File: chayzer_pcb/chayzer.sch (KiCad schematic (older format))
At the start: 30 parts, among them U1 ProMicro

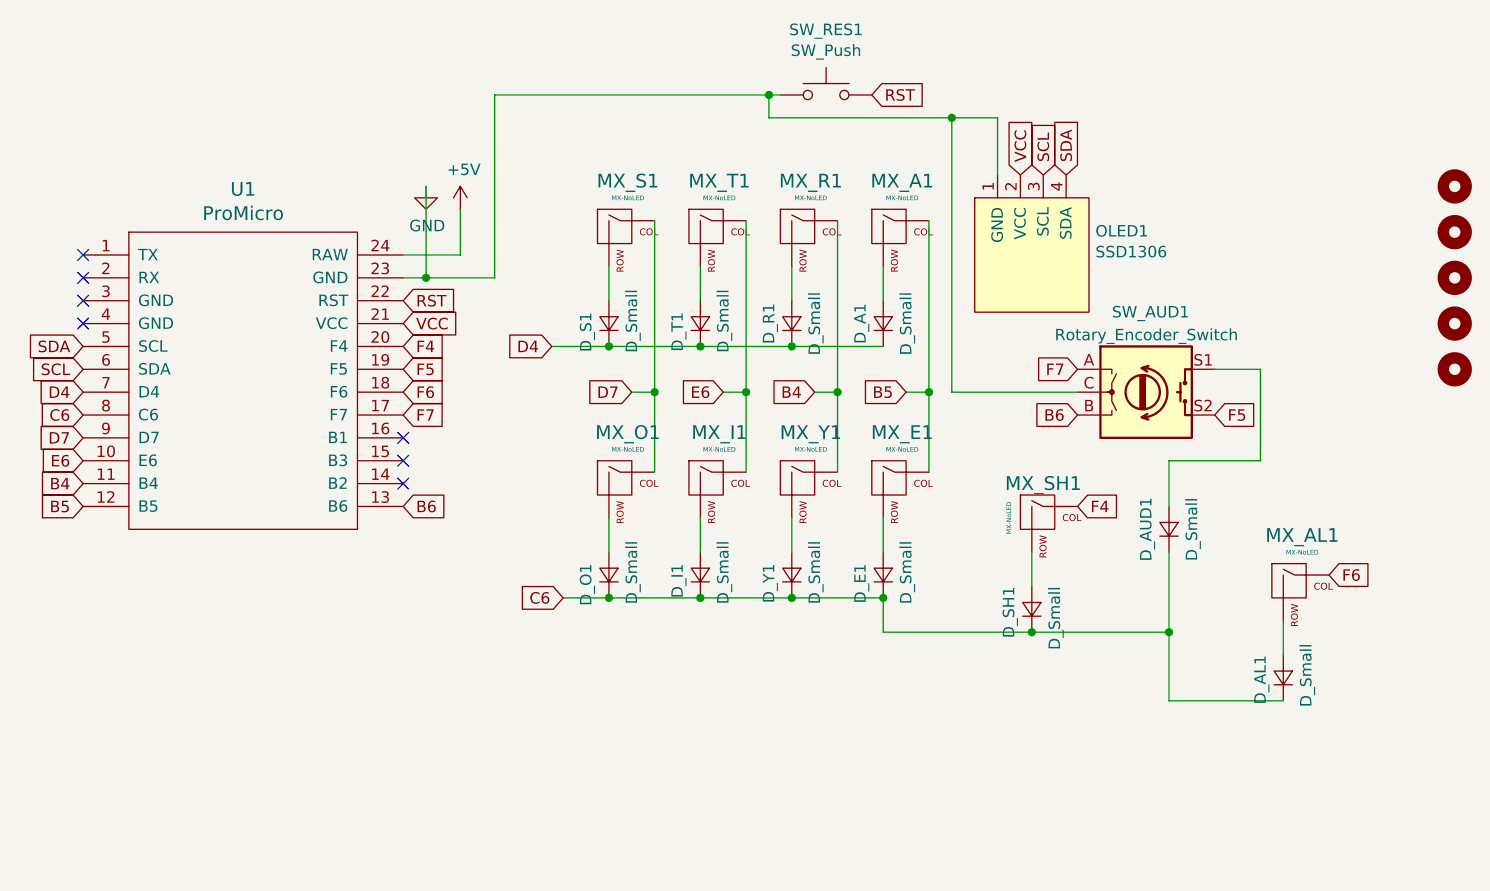
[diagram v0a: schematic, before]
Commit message: added rgb to PCB, buggy in qmk right now, and untested on PCB
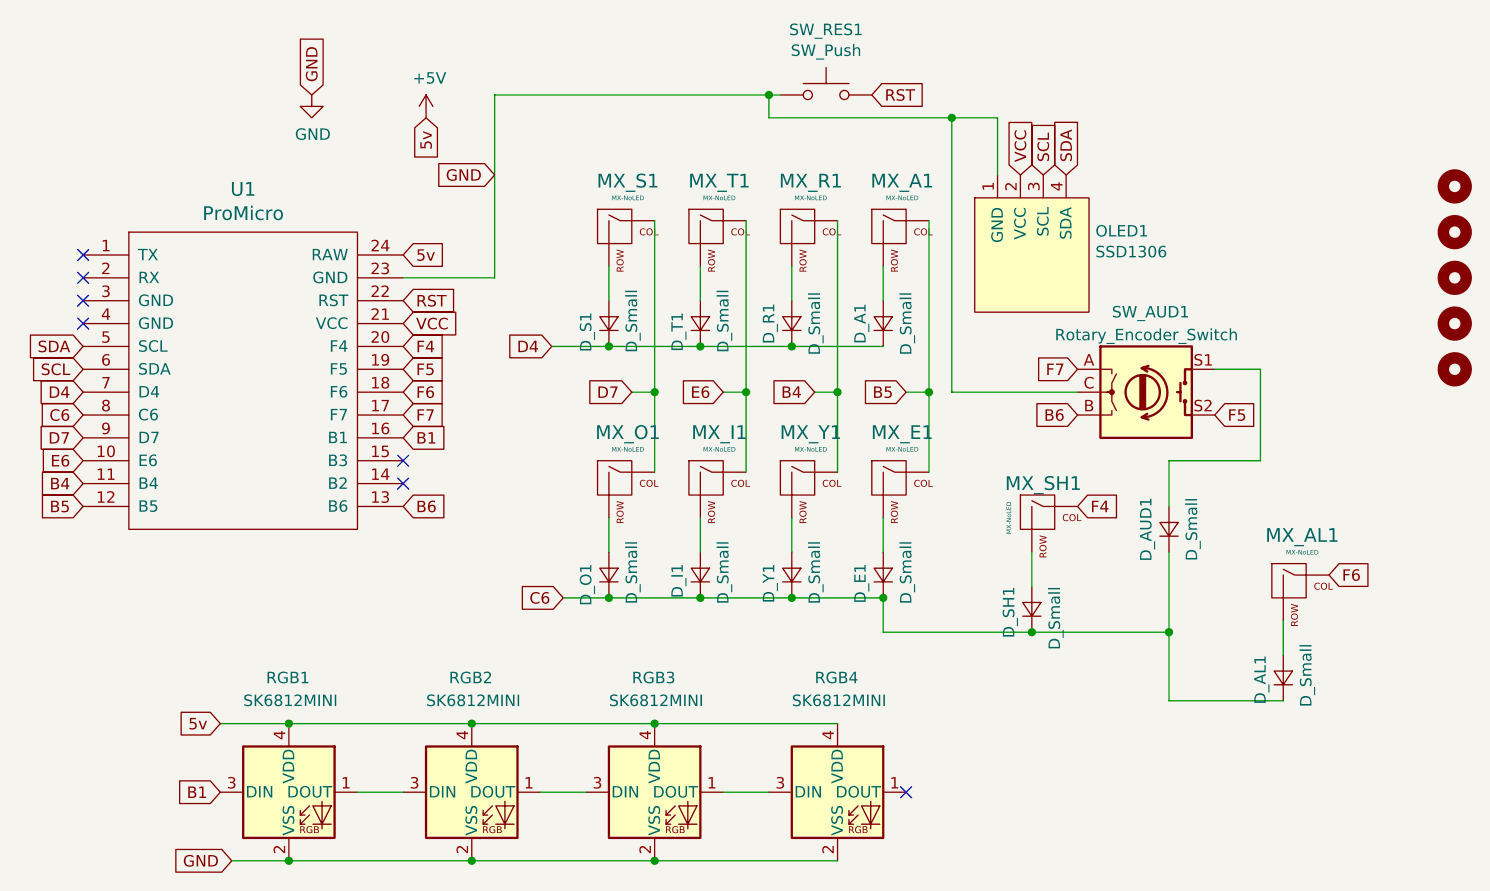
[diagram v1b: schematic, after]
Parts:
- added RGB1, RGB2, RGB3, RGB4: SK6812MINI, LED_SMD:LED_SK6812MINI_PLCC4_3.5x3.5mm_P1.75mm, symbol LED:SK6812MINI
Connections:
- net +5V: now also RGB1.4 (VDD), RGB2.4 (VDD), RGB3.4 (VDD), RGB4.4 (VDD)
- net GND: now also RGB1.2 (VSS), RGB2.2 (VSS), RGB3.2 (VSS), RGB4.2 (VSS)
- net B1: now reaches U1.16 (B1)
- net B1: now also RGB1.3 (DIN)
- new net: RGB1.1 (DOUT), RGB2.3 (DIN)
- new net: RGB2.1 (DOUT), RGB3.3 (DIN)
- new net: RGB3.1 (DOUT), RGB4.3 (DIN)
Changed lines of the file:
@@
 EESchema Schematic File Version 4
+LIBS:chayzer-cache
 EELAYER 30 0
 EELAYER END
@@
 $EndDescr
 $Comp
-L power:+5V #PWR0101
-U 1 1 60D53ACC
-P 4700 3000
-F 0 "#PWR0101" H 4700 2850 50  0001 C CNN
-F 1 "+5V" H 4715 3173 50  0000 C CNN
-F 2 "" H 4700 3000 50  0001 C CNN
-F 3 "" H 4700 3000 50  0001 C CNN
-	1    4700 3000
-	1    0    0    -1
-$EndComp
-$Comp
 L chayzer-rescue:ProMicro-promicro U1
 U 1 1 60D57CF4
@@
 L power:GND #PWR0102
 U 1 1 60D5522F
-P 4550 2900
-F 0 "#PWR0102" H 4550 2650 50  0001 C CNN
-F 1 "GND" H 4555 2727 50  0000 C CNN
-F 2 "" H 4550 2900 50  0001 C CNN
-F 3 "" H 4550 2900 50  0001 C CNN
-	1    4550 2900
-	1    0    0    -1
-$EndComp
-Wire Wire Line
-	4700 3000 4700 3200
-Wire Wire Line
-	4700 3200 4450 3200
+P 4050 2500
+F 0 "#PWR0102" H 4050 2250 50  0001 C CNN
+F 1 "GND" H 4055 2327 50  0000 C CNN
+F 2 "" H 4050 2500 50  0001 C CNN
+F 3 "" H 4050 2500 50  0001 C CNN
+	1    4050 2500
+	1    0    0    -1
+$EndComp
 $Comp
 L chayzer-rescue:MX-NoLED-MX_Alps_Hybrid MX_S1
@@
 	6050 2500 4850 2500
 Wire Wire Line
-	4450 3300 4550 3300
-Wire Wire Line
-	4550 2900 4550 3300
-Connection ~ 4550 3300
-Wire Wire Line
-	4550 3300 4850 3300
-Wire Wire Line
 	5350 3250 5350 3400
 Wire Wire Line
@@
 NoConn ~ 4450 4200
 NoConn ~ 4450 4100
-NoConn ~ 4450 4000
 Wire Wire Line
 	5100 3600 5350 3600
@@
 Text GLabel 4450 4300 2    50   Input ~ 0
 B6
+$Comp
+L LED:SK6812MINI RGB1
+U 1 1 61032E51
+P 3950 5550
+F 0 "RGB1" H 3850 6050 50  0000 L CNN
+F 1 "SK6812MINI" H 3750 5950 50  0000 L CNN
+F 2 "LED_SMD:LED_SK6812MINI_PLCC4_3.5x3.5mm_P1.75mm" H 4000 5250 50  0001 L TNN
+F 3 "https://cdn-shop.adafruit.com/product-files/2686/SK6812MINI_REV.01-1-2.pdf" H 4050 5175 50  0001 L TNN
+	1    3950 5550
+	1    0    0    -1
+$EndComp
+Wire Wire Line
+	4450 3300 4850 3300
+$Comp
+L power:+5V #PWR0101
+U 1 1 60D53ACC
+P 4550 2600
+F 0 "#PWR0101" H 4550 2450 50  0001 C CNN
+F 1 "+5V" H 4565 2773 50  0000 C CNN
+F 2 "" H 4550 2600 50  0001 C CNN
+F 3 "" H 4550 2600 50  0001 C CNN
+	1    4550 2600
+	1    0    0    -1
+$EndComp
+Text GLabel 4450 3200 2    50   Input ~ 0
+5v
+Text GLabel 4850 2850 0    50   Input ~ 0
+GND
+Text GLabel 4550 2600 3    50   Input ~ 0
+5v
+Text GLabel 4050 2500 1    50   Input ~ 0
+GND
+$Comp
+L LED:SK6812MINI RGB2
+U 1 1 6103E43F
+P 4750 5550
+F 0 "RGB2" H 4650 6050 50  0000 L CNN
+F 1 "SK6812MINI" H 4550 5950 50  0000 L CNN
+F 2 "LED_SMD:LED_SK6812MINI_PLCC4_3.5x3.5mm_P1.75mm" H 4800 5250 50  0001 L TNN
+F 3 "https://cdn-shop.adafruit.com/product-files/2686/SK6812MINI_REV.01-1-2.pdf" H 4850 5175 50  0001 L TNN
+	1    4750 5550
+	1    0    0    -1
+$EndComp
+$Comp
+L LED:SK6812MINI RGB3
+U 1 1 6103F28F
+P 5550 5550
+F 0 "RGB3" H 5450 6050 50  0000 L CNN
+F 1 "SK6812MINI" H 5350 5950 50  0000 L CNN
+F 2 "LED_SMD:LED_SK6812MINI_PLCC4_3.5x3.5mm_P1.75mm" H 5600 5250 50  0001 L TNN
+F 3 "https://cdn-shop.adafruit.com/product-files/2686/SK6812MINI_REV.01-1-2.pdf" H 5650 5175 50  0001 L TNN
+	1    5550 5550
+	1    0    0    -1
+$EndComp
+$Comp
+L LED:SK6812MINI RGB4
+U 1 1 6103FF53
+P 6350 5550
+F 0 "RGB4" H 6250 6050 50  0000 L CNN
+F 1 "SK6812MINI" H 6150 5950 50  0000 L CNN
+F 2 "LED_SMD:LED_SK6812MINI_PLCC4_3.5x3.5mm_P1.75mm" H 6400 5250 50  0001 L TNN
+F 3 "https://cdn-shop.adafruit.com/product-files/2686/SK6812MINI_REV.01-1-2.pdf" H 6450 5175 50  0001 L TNN
+	1    6350 5550
+	1    0    0    -1
+$EndComp
+Text GLabel 4450 4000 2    50   Input ~ 0
+B1
+Text GLabel 3650 5550 0    50   Input ~ 0
+B1
+Wire Wire Line
+	4250 5550 4450 5550
+Wire Wire Line
+	5050 5550 5250 5550
+Wire Wire Line
+	5850 5550 6050 5550
+NoConn ~ 6650 5550
+Text GLabel 3700 5850 0    50   Input ~ 0
+GND
+Wire Wire Line
+	3700 5850 3950 5850
+Connection ~ 3950 5850
+Wire Wire Line
+	3950 5850 4750 5850
+Connection ~ 4750 5850
+Wire Wire Line
+	4750 5850 5550 5850
+Connection ~ 5550 5850
+Wire Wire Line
+	5550 5850 6350 5850
+Text GLabel 3650 5250 0    50   Input ~ 0
+5v
+Wire Wire Line
+	3650 5250 3950 5250
+Connection ~ 3950 5250
+Wire Wire Line
+	3950 5250 4750 5250
+Connection ~ 4750 5250
+Wire Wire Line
+	4750 5250 5550 5250
+Connection ~ 5550 5250
+Wire Wire Line
+	5550 5250 6350 5250
 $EndSCHEMATC
